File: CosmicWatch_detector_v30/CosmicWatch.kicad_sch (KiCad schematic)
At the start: 102 parts, among them J3 RJ45, P1 CONN_01X04, P10 CONN_02X02, P11 CONN_01X01, P12 CONN_01X01, P13 CONN_01X01, P14 CONN_01X01, P15 CONN_02X04, P16 CONN_01X02, P19 CONN_01X01, P2 CONN_01X01, P3 CONN_01X04, P4 CONN_01X04, P5 CONN_01X02, P7 CONN_01X01, P8 CONN_01X01, SW1 RESET, U1 MAX5026, U12 LTC6752, U13 TS5A1066, U16 UMCC, U17 UMCC, U19 LMH6658, U2 SiPM_MicroFJ−300XX−TSV, U22 UMCC, U23 UMCC, U3 MMCX, U4 TS5A1066, U5 RasberryPi_Pico, U6 LMH6658, U7 TPS6040X, U8 sd_card_socket, U9 2NPNMBT6429DW1T1G

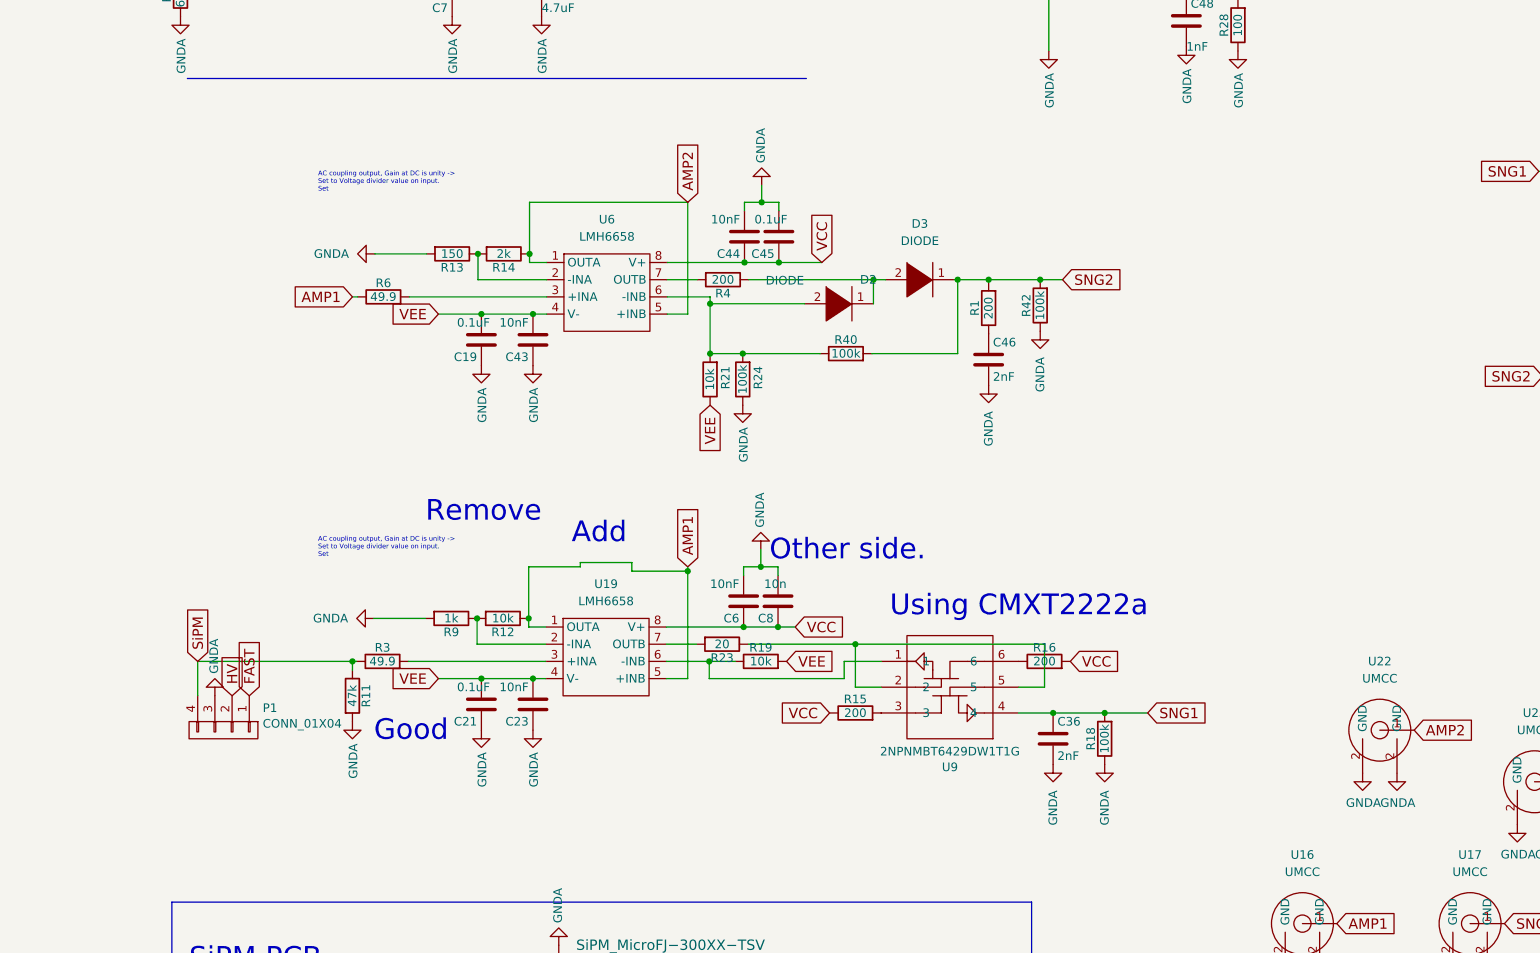
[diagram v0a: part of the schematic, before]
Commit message: adding peak detector and comparator
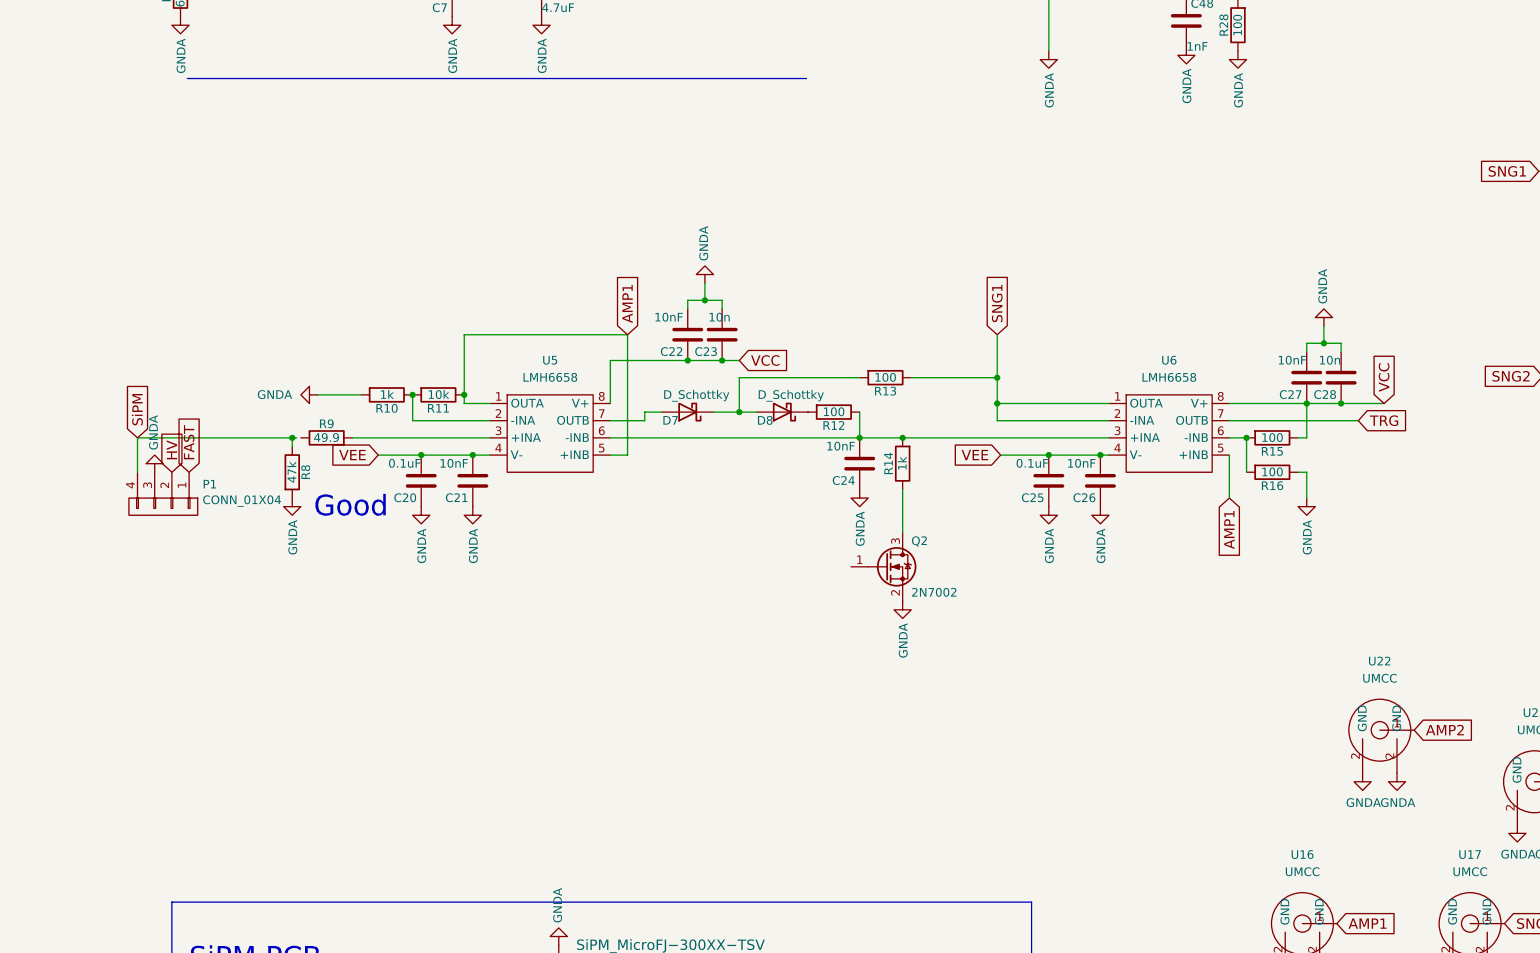
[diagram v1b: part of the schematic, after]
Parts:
- removed C19, C45: 0.1uF, Capacitor_SMD:C_0603_1608Metric, symbol device:C
- removed C36, C46: 2nF, Capacitor_SMD:C_0603_1608Metric, symbol device:C
- removed C43, C44, C6: 10nF, Capacitor_SMD:C_0603_1608Metric, symbol device:C
- removed C8: 10n, Capacitor_SMD:C_0603_1608Metric, symbol device:C
- removed D2, D3: DIODE, Diode_SMD:D_SOD-123, symbol pspice:DIODE
- removed R1, R4: 200, Capacitor_SMD:C_0603_1608Metric, symbol device:R
- removed R18, R24, R40, R42: 100k, Capacitor_SMD:C_0603_1608Metric, symbol device:R
- removed R19, R21: 10k, Capacitor_SMD:C_0603_1608Metric, symbol device:R
- removed R23: 20, Capacitor_SMD:C_0603_1608Metric, symbol device:R
- removed R3, R6: 49.9, Capacitor_SMD:C_0603_1608Metric, symbol device:R
- removed U19: LMH6658, Package_SO:SOIC-8_3.9x4.9mm_P1.27mm, symbol My_Library:LMH6658
- removed U9: 2NPNMBT6429DW1T1G, Package_TO_SOT_SMD:SOT-23-6, symbol MyLibrary:2NPNMBT6429DW1T1G
- added C20, C25: 0.1uF, Capacitor_SMD:C_0603_1608Metric, symbol device:C
- added C22, C24, C26, C27: 10nF, Capacitor_SMD:C_0603_1608Metric, symbol device:C
- added C28: 10n, Capacitor_SMD:C_0603_1608Metric, symbol device:C
- added D7, D8: D_Schottky, Diode_SMD:D_SOD-523, symbol My_Symbol_Library:D_Schottky
- added Q2: 2N7002, Package_TO_SOT_SMD:SOT-23, symbol Transistor_FET:2N7002
- added R10: 1k, Capacitor_SMD:C_0603_1608Metric, symbol device:R
- added R8: 47k, Capacitor_SMD:C_0603_1608Metric, symbol device:R
- added U5: LMH6658, Package_SO:SOIC-8_3.9x4.9mm_P1.27mm, symbol My_Library:LMH6658
- C21: value 0.1uF -> 10nF
- C23: value 10nF -> 10n
- R11: value 47k -> 10k
- R12: value 10k -> 100
- R13: value 150 -> 100
- R14: value 2k -> 1k
- R15, R16: value 200 -> 100
- R9: value 1k -> 49.9
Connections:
- net AMP1: now also R11.1, U6.5 (+INB), U5.1 (OUTA), U5.5 (+INB); no longer R12.1
- net AMP2: no longer R14.1, U6.1 (OUTA), U6.5 (+INB)
- net GNDA: now also C23.2, R16.1, C20.1, C22.2, C24.1, C25.1, C26.1, C27.2, C28.2, Q2.2 (S), R10.2, R8.2; no longer C23.1, R11.2, R13.2, R9.2
- net SNG1: now also R13.1, U6.1 (OUTA), U6.2 (-INA)
- net SiPM: now also R8.1; no longer R11.1
- net TRG: now also U6.7 (OUTB)
- net VCC: now also C23.1, C22.1, C27.1, C28.1, U5.8 (V+); no longer R16.2
- net VEE: now also C20.2, C25.2, C26.2, U5.4 (V-); no longer C23.2
- net at R15.2: now also R16.2, U6.6 (-INB)
- net at R12.2: now also D8.1 (K); no longer R9.1
- net at U6.3 (+INA): now also R12.1, R14.2, C24.2, U5.6 (-INB)
- new net: D7.1 (K), D8.2 (A), R13.2
- new net: R9.2, U5.3 (+INA)
- new net: Q2.3 (D), R14.1
- new net: R10.1, R11.2, U5.2 (-INA)
- new net: D7.2 (A), U5.7 (OUTB)
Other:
- note removed: "AC coupling output, Gain at DC is unity -> Set to Voltage divider value on input. Set"
- note removed: "Add"
- note removed: "Other side."
- note removed: "Remove"
- note removed: "Using CMXT2222a"

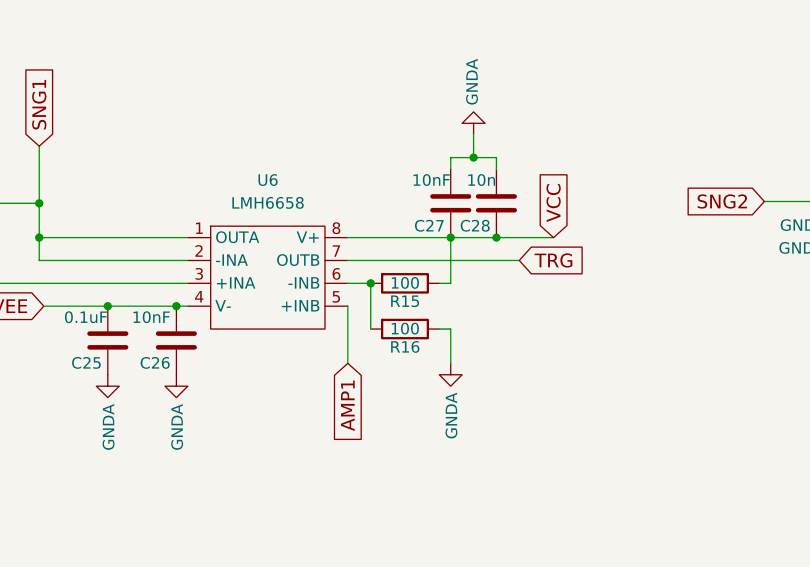
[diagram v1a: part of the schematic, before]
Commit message: fixing R13 resistance value
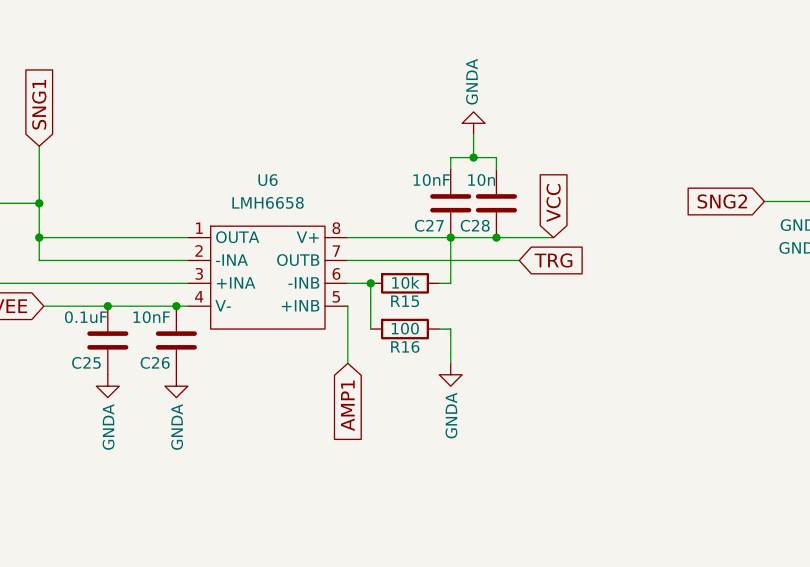
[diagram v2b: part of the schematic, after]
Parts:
- R15: value 100 -> 10k
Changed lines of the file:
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@@
       (effects (font (size 1.27 1.27)))
     )
-    (property "Value" "100" (at 189.23 125.73 90)
+    (property "Value" "10k" (at 189.23 125.73 90)
       (effects (font (size 1.27 1.27)))
     )

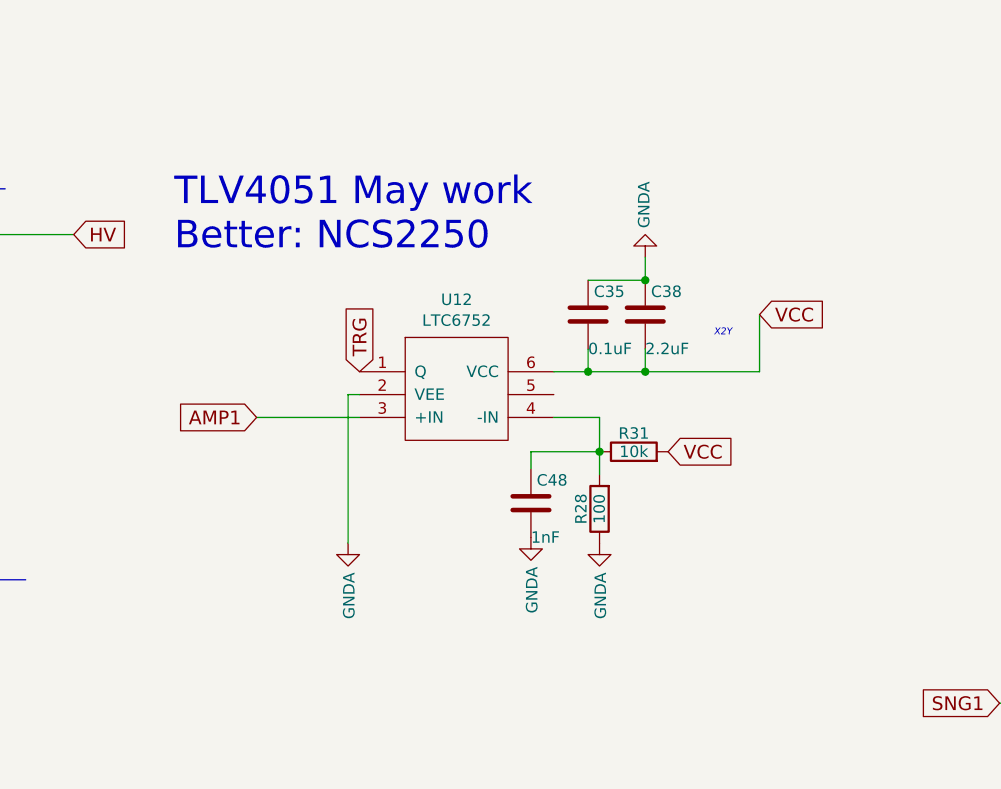
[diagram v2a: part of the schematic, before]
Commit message: removig old comparator
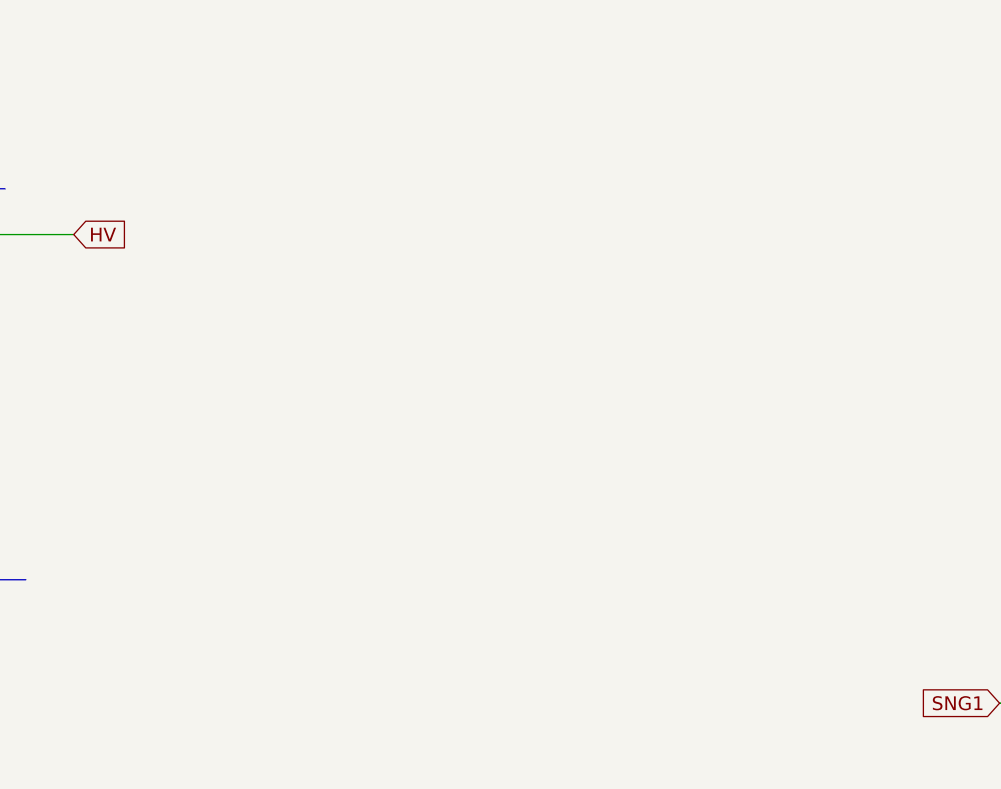
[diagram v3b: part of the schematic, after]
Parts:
- removed C35: 0.1uF, Capacitor_SMD:C_0603_1608Metric, symbol device:C
- removed C38: 2.2uF, Capacitor_SMD:C_0603_1608Metric, symbol device:C
- removed C48: 1nF, Capacitor_SMD:C_0603_1608Metric, symbol device:C
- removed R28: 100, Capacitor_SMD:C_0603_1608Metric, symbol device:R
- removed R31: 10k, Capacitor_SMD:C_0603_1608Metric, symbol device:R
- removed U12: LTC6752, Package_TO_SOT_SMD:SOT-23-6, symbol MyLibrary:LTC6752
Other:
- note removed: "TLV4051 May work Better: NCS2250"
- note removed: "X2Y"
